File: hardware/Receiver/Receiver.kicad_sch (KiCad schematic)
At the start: 120 parts, among them IC1 ESP32-C3-MINI-1-N4, J1 USB_C_Receptacle_USB2.0, J3 20021511-00006T4LF, J4 Conn_01x04, J6 JST_PH, Q1 2N7002, Q10 NChan, Q11 NChan, Q2 NChan, Q3 NChan, Q4 NChan, Q5 PChan, Q6 PChan, Q7 PChan, Q8 NChan, Q9 NChan, SW1 Reset, SW2 1825027-8, U1 TPS22810DRV, U2 DMG6602SVTQ, U2 TPS22810DRV, U3 AZ1117-3.3, U3 DMG6602SVTQ, U4 TLV493DA1B6HTSA2

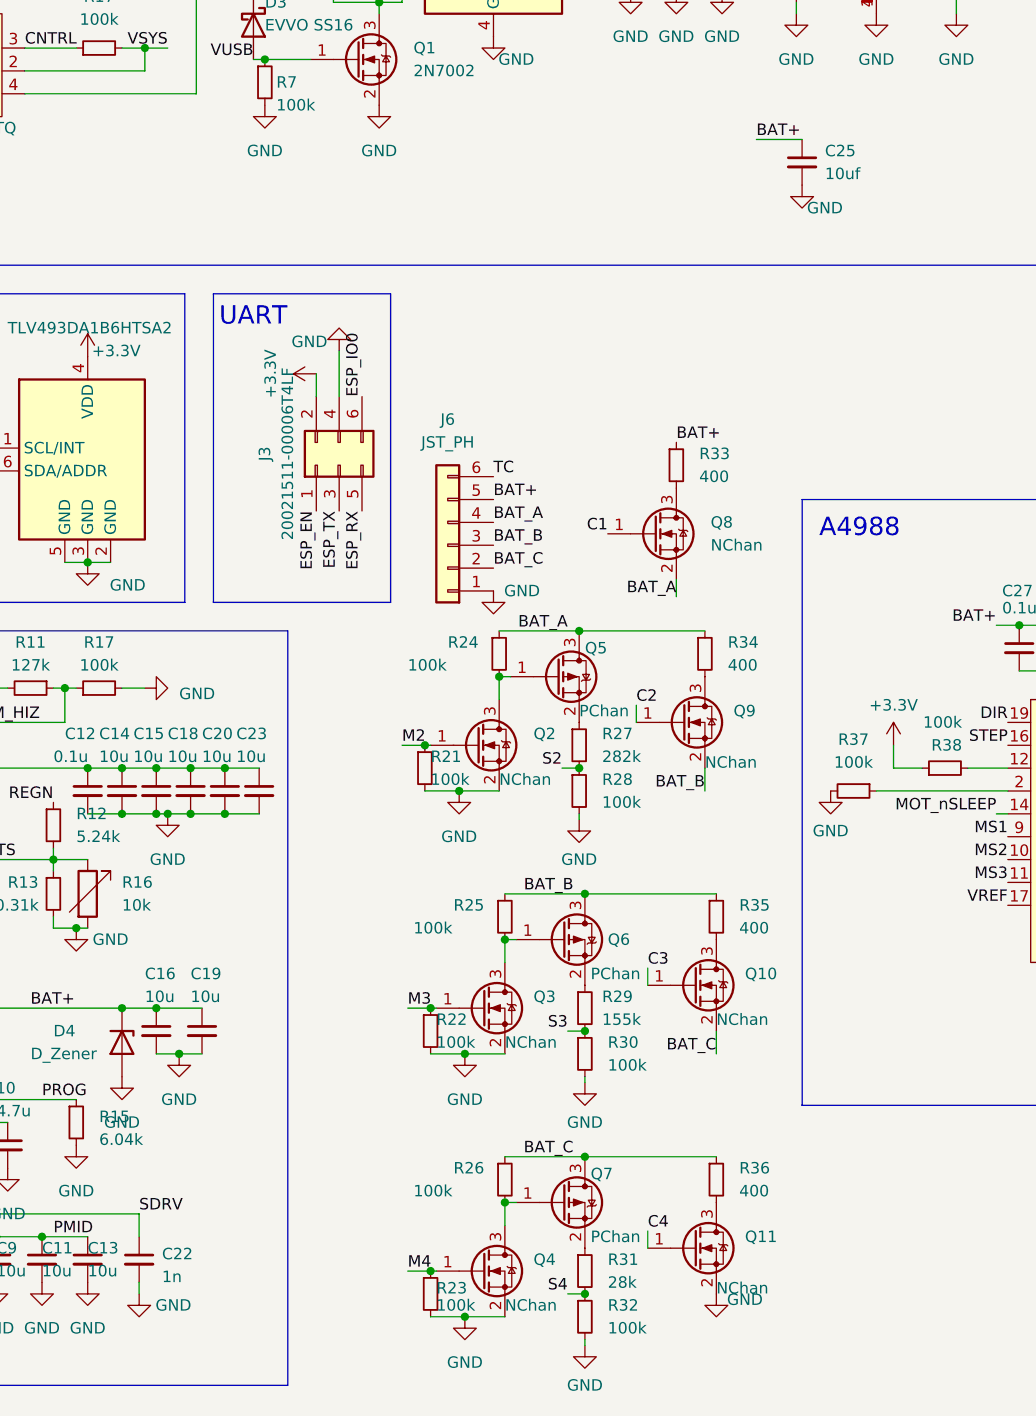
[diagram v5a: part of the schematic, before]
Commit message: rename battery leads, update footprints
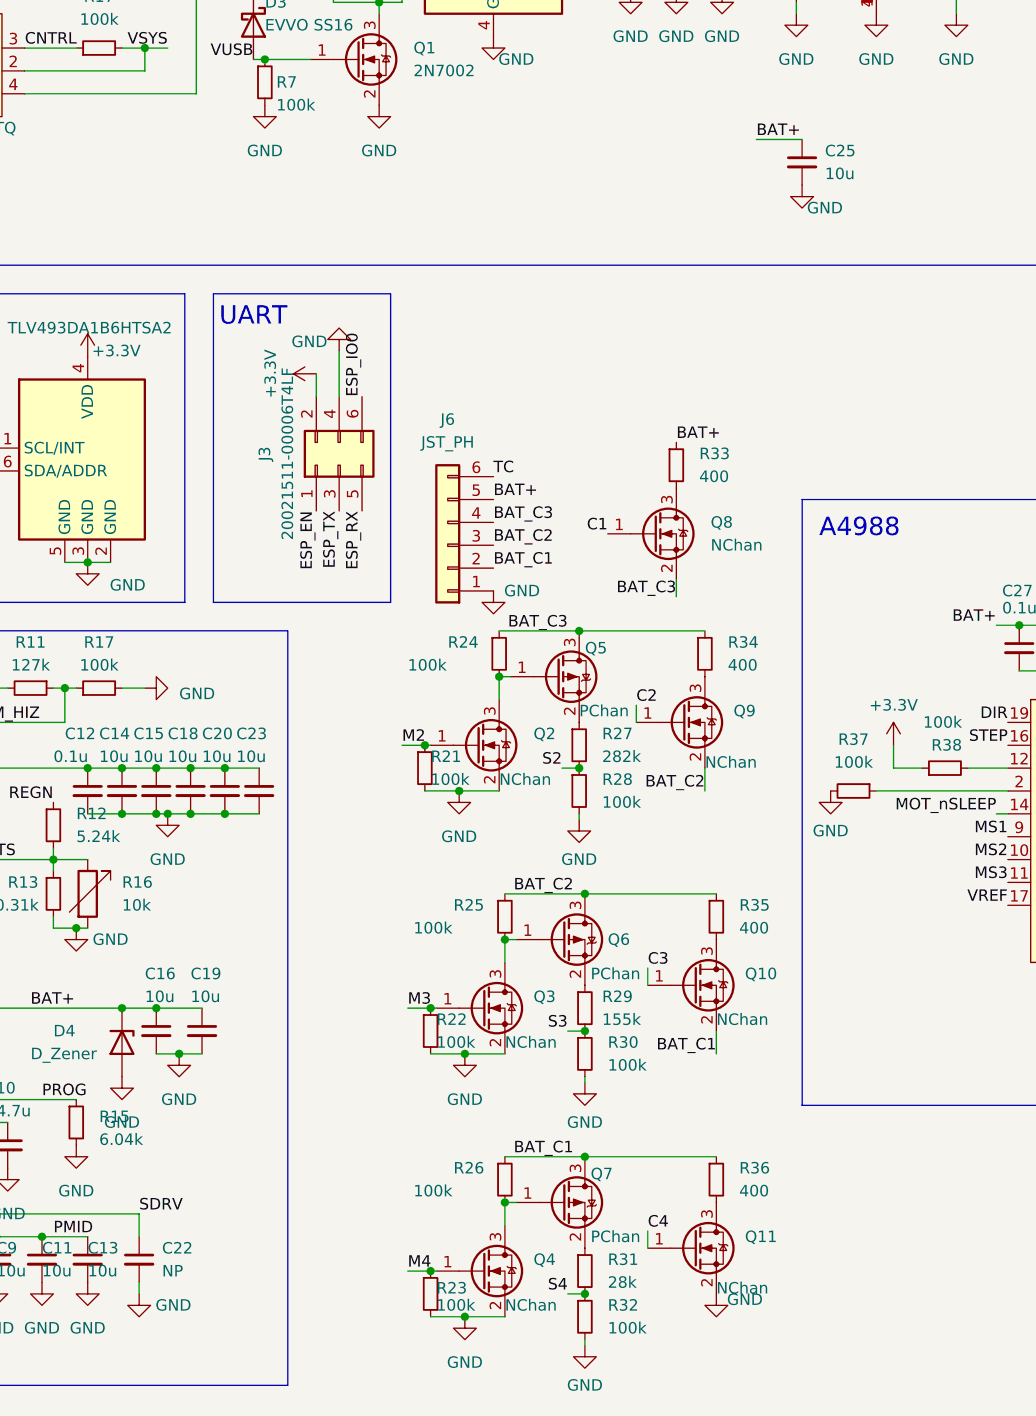
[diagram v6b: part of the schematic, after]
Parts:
- C17, C27: footprint Capacitor_SMD:C_0402_1005Metric -> Capacitor_SMD:C_0603_1608Metric
- C22: value 1n -> NP
- C25: value 10uf -> 10u; footprint Capacitor_SMD:C_0402_1005Metric -> Capacitor_SMD:C_0603_1608Metric
- C28: footprint Capacitor_SMD:C_0402_1005Metric -> Capacitor_SMD:C_0805_2012Metric
- R18, R19, R7, R8: footprint Capacitor_SMD:C_0402_1005Metric -> Resistor_SMD:R_0402_1005Metric
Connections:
- net BAT_A renamed BAT_C3
- net BAT_B renamed BAT_C2
- net BAT_C renamed BAT_C1
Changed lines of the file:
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@@
     (effects (font (size 1.27 1.27)) (justify left bottom))
   )
-  (label "BAT_A" (at 150.495 111.125 180) (fields_autoplaced)
+  (label "BAT_C3" (at 150.495 111.125 180) (fields_autoplaced)
     (effects (font (size 1.27 1.27)) (justify right bottom))
   )
@@
     (effects (font (size 1.27 1.27)) (justify left bottom))
   )
-  (label "BAT_C" (at 151.13 169.545 180) (fields_autoplaced)
+  (label "BAT_C1" (at 151.13 169.545 180) (fields_autoplaced)
     (effects (font (size 1.27 1.27)) (justify right bottom))
   )
@@
     (effects (font (size 1.27 1.27)) (justify left bottom))
   )
-  (label "BAT_B" (at 165.735 128.905 180) (fields_autoplaced)
+  (label "BAT_C2" (at 165.735 128.905 180) (fields_autoplaced)
     (effects (font (size 1.27 1.27)) (justify right bottom))
   )
@@
     (effects (font (size 1.27 1.27)) (justify right bottom))
   )
-  (label "BAT_C" (at 167.005 158.115 180) (fields_autoplaced)
+  (label "BAT_C1" (at 167.005 158.115 180) (fields_autoplaced)
     (effects (font (size 1.27 1.27)) (justify right bottom))
   )
@@
     (effects (font (size 1.27 1.27)) (justify left bottom))
   )
-  (label "BAT_A" (at 162.56 107.315 180) (fields_autoplaced)
+  (label "BAT_C3" (at 162.56 107.315 180) (fields_autoplaced)
     (effects (font (size 1.27 1.27)) (justify right bottom))
   )
@@
     (effects (font (size 1.27 1.27)) (justify left bottom))
   )
-  (label "BAT_A" (at 142.24 99.06 0) (fields_autoplaced)
+  (label "BAT_C3" (at 142.24 99.06 0) (fields_autoplaced)
     (effects (font (size 1.27 1.27)) (justify left bottom))
   )
-  (label "BAT_C" (at 142.24 104.14 0) (fields_autoplaced)
+  (label "BAT_C1" (at 142.24 104.14 0) (fields_autoplaced)
     (effects (font (size 1.27 1.27)) (justify left bottom))
   )
@@
     (effects (font (size 1.27 1.27)) (justify right bottom))
   )
-  (label "BAT_B" (at 151.13 140.335 180) (fields_autoplaced)
+  (label "BAT_C2" (at 151.13 140.335 180) (fields_autoplaced)
     (effects (font (size 1.27 1.27)) (justify right bottom))
   )
@@
     (effects (font (size 1.27 1.27)) (justify right bottom))
   )
-  (label "BAT_B" (at 142.24 101.6 0) (fields_autoplaced)
+  (label "BAT_C2" (at 142.24 101.6 0) (fields_autoplaced)
     (effects (font (size 1.27 1.27)) (justify left bottom))
   )
@@
   (symbol (lib_id "Device:C_Small") (at 102.87 180.975 0) (unit 1)
     (in_bom yes) (on_board yes) (dnp no) (fields_autoplaced)
-    (property "Reference" "C22" (at 105.41 180.3463 0)
+    (property "Reference" "C22" (at 105.41 179.7113 0)
       (effects (font (size 1.27 1.27)) (justify left))
     )
-    (property "Value" "1n" (at 105.41 182.8863 0)
+    (property "Value" "NP" (at 105.41 182.2513 0)
       (effects (font (size 1.27 1.27)) (justify left))
     )
@@
       (effects (font (size 1.27 1.27)) (justify left))
     )
-    (property "Footprint" "Capacitor_SMD:C_0402_1005Metric" (at 116.84 50.165 0)
+    (property "Footprint" "Resistor_SMD:R_0402_1005Metric" (at 116.84 50.165 0)
       (effects (font (size 1.27 1.27)) hide)
     )
@@
       (effects (font (size 1.27 1.27)) (justify left))
     )
-    (property "Footprint" "Capacitor_SMD:C_0402_1005Metric" (at 157.48 37.465 0)
+    (property "Footprint" "Capacitor_SMD:C_0603_1608Metric" (at 157.48 37.465 0)
       (effects (font (size 1.27 1.27)) hide)
     )
@@
       (effects (font (size 1.27 1.27)) (justify left))
     )
-    (property "Footprint" "Capacitor_SMD:C_0402_1005Metric" (at 193.675 37.465 0)
+    (property "Footprint" "Capacitor_SMD:C_0805_2012Metric" (at 193.675 37.465 0)
       (effects (font (size 1.27 1.27)) hide)
     )
@@
       (effects (font (size 1.27 1.27)) (justify right))
     )
-    (property "Footprint" "Capacitor_SMD:C_0402_1005Metric" (at 124.46 37.465 0)
+    (property "Footprint" "Resistor_SMD:R_0402_1005Metric" (at 124.46 37.465 0)
       (effects (font (size 1.27 1.27)) hide)
     )
@@
       (effects (font (size 1.27 1.27)) (justify left))
     )
-    (property "Footprint" "Capacitor_SMD:C_0402_1005Metric" (at 219.075 60.96 0)
+    (property "Footprint" "Resistor_SMD:R_0402_1005Metric" (at 219.075 60.96 0)
       (effects (font (size 1.27 1.27)) hide)
     )
@@
       (effects (font (size 1.27 1.27)) (justify left))
     )
-    (property "Footprint" "Capacitor_SMD:C_0402_1005Metric" (at 175.895 38.735 0)
+    (property "Footprint" "Capacitor_SMD:C_0603_1608Metric" (at 175.895 38.735 0)
       (effects (font (size 1.27 1.27)) hide)
     )
@@
       (effects (font (size 1.27 1.27)) (justify left))
     )
-    (property "Footprint" "Capacitor_SMD:C_0402_1005Metric" (at 211.455 60.96 0)
+    (property "Footprint" "Resistor_SMD:R_0402_1005Metric" (at 211.455 60.96 0)
       (effects (font (size 1.27 1.27)) hide)
     )
@@
       (effects (font (size 1.27 1.27)) (justify left))
     )
-    (property "Value" "10uf" (at 179.07 60.3313 0)
+    (property "Value" "10u" (at 179.07 60.3313 0)
       (effects (font (size 1.27 1.27)) (justify left))
     )
-    (property "Footprint" "Capacitor_SMD:C_0402_1005Metric" (at 176.53 59.055 0)
+    (property "Footprint" "Capacitor_SMD:C_0603_1608Metric" (at 176.53 59.055 0)
       (effects (font (size 1.27 1.27)) hide)
     )
